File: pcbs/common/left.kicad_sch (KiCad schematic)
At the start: 88 parts

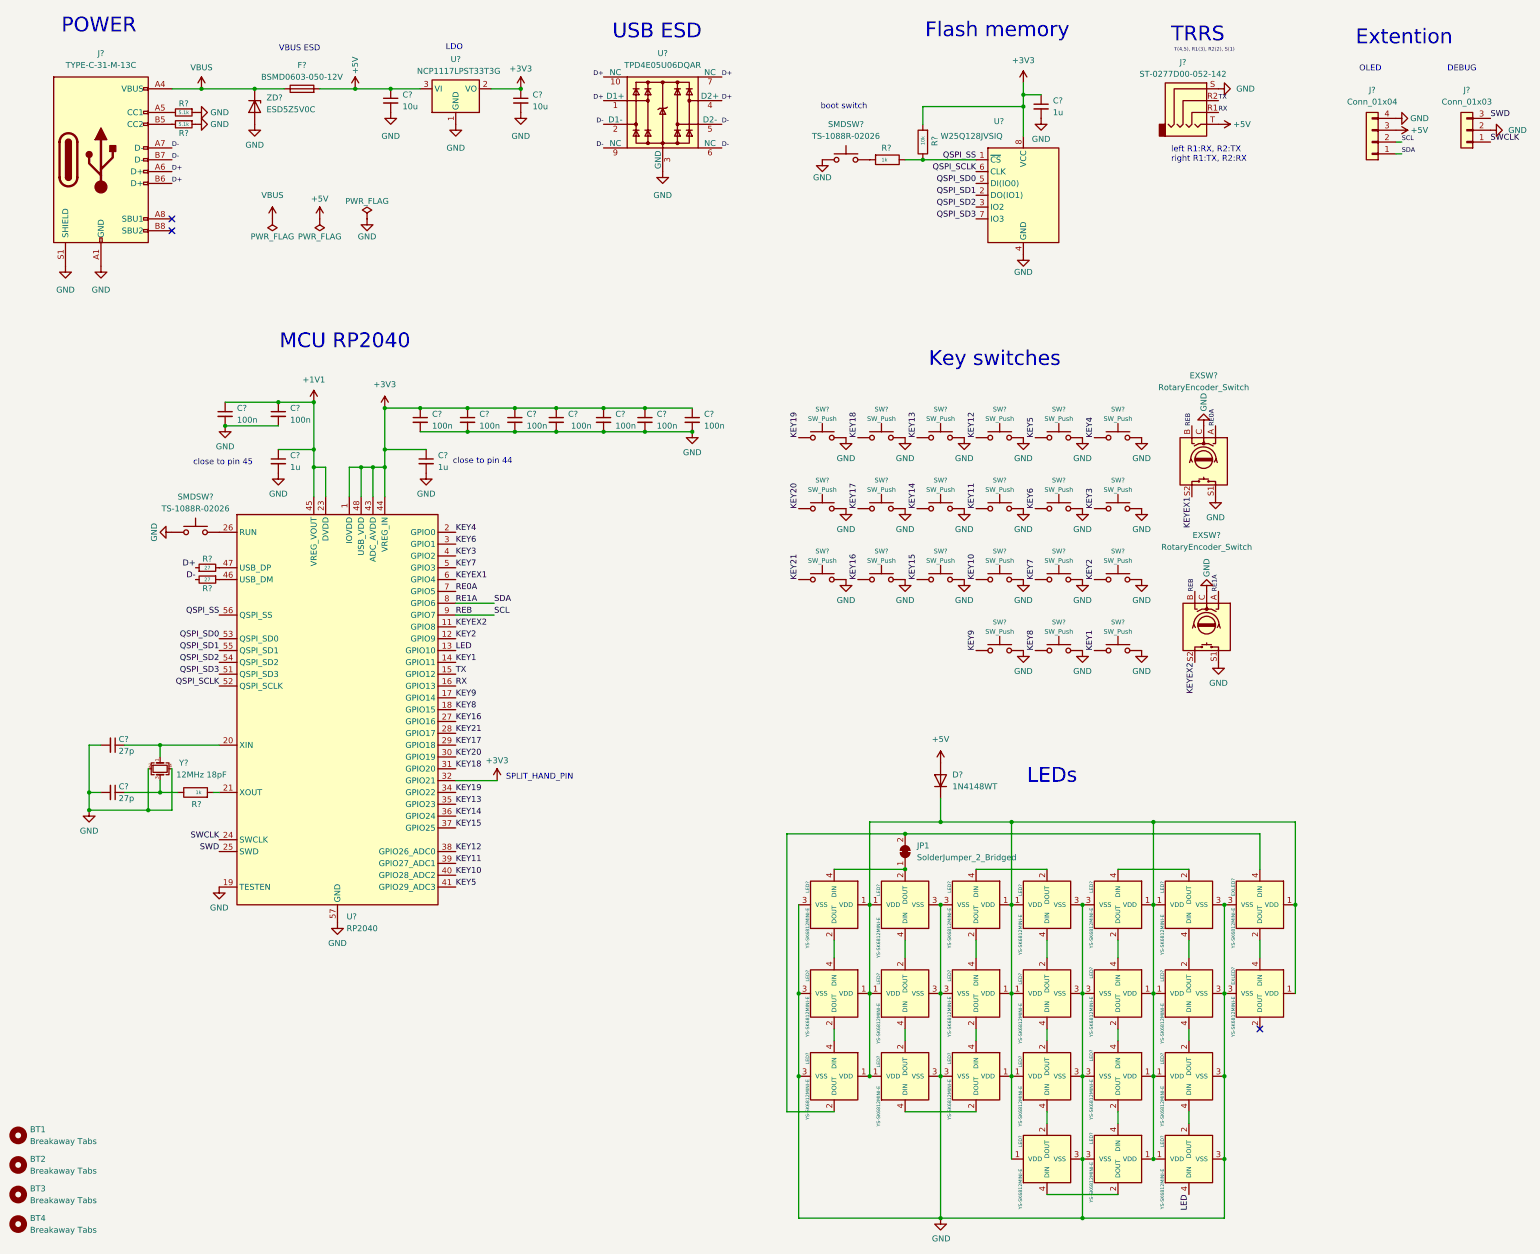
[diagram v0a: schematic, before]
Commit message: Updated pcb for corne-chocolate to use PJ-606-6A audio jack
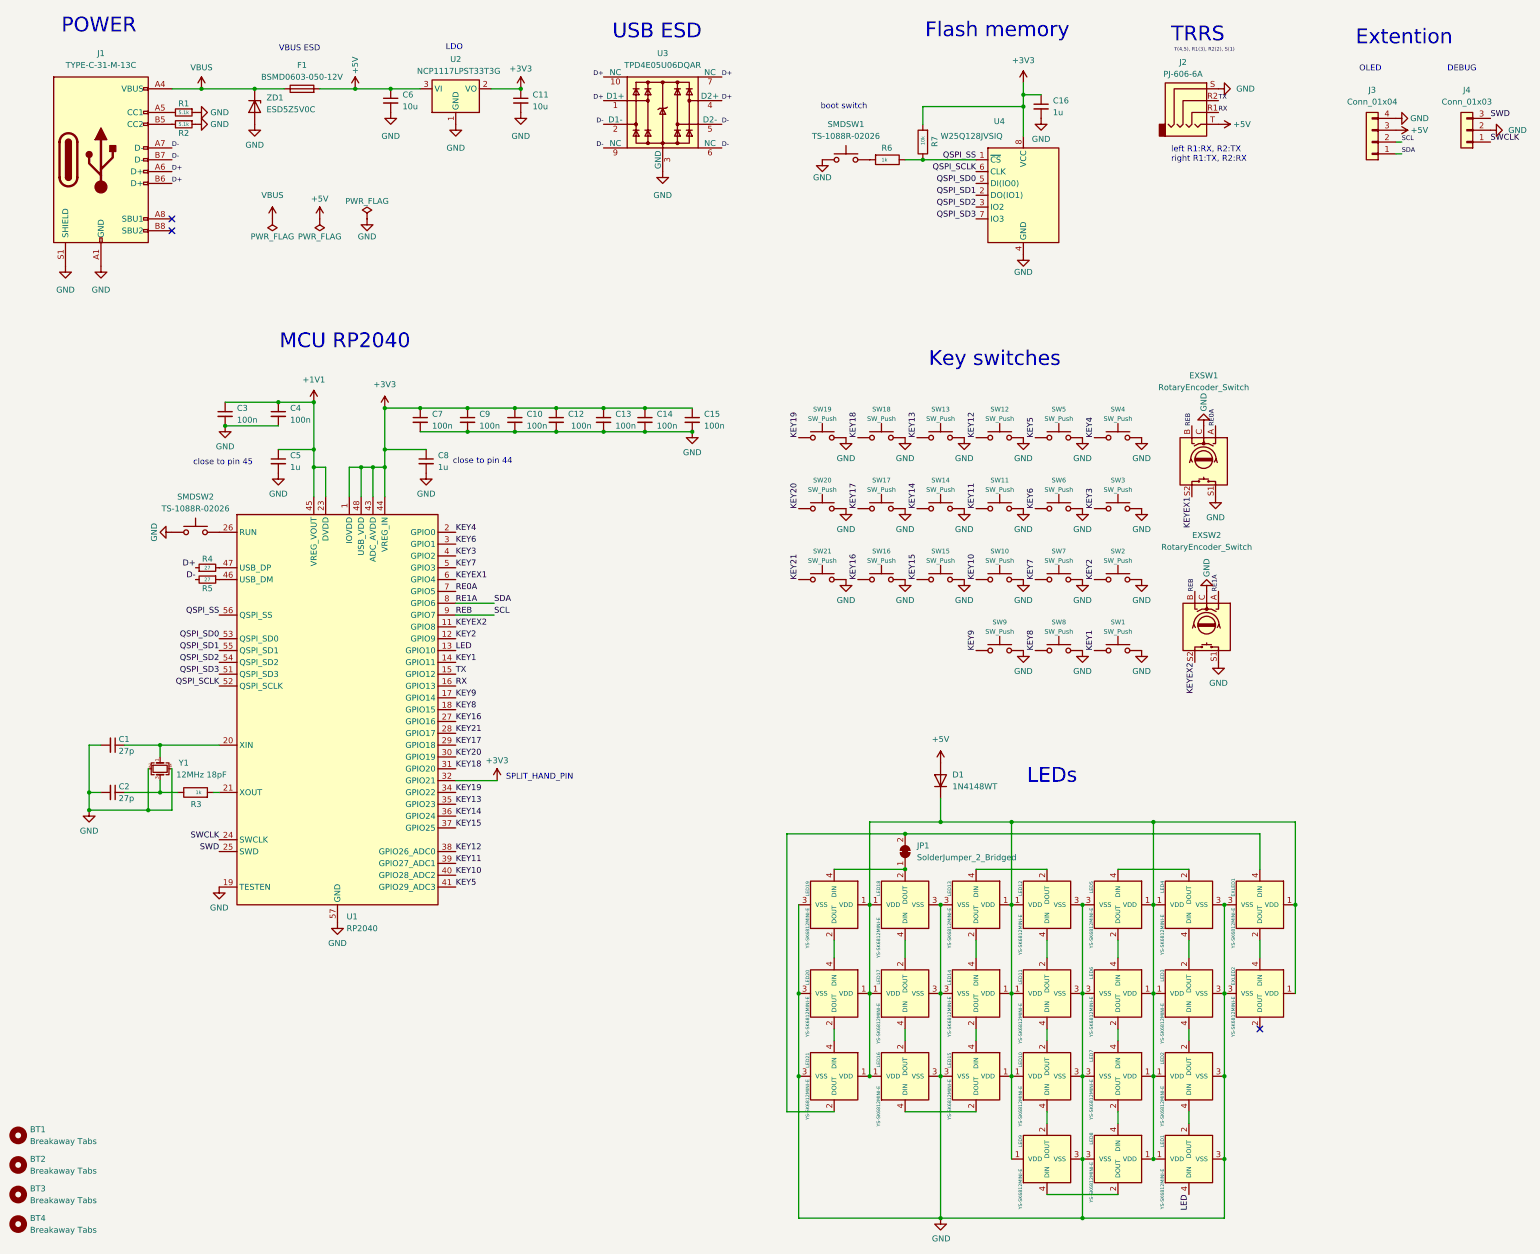
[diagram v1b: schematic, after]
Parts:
- EXLED1, EXLED2: renamed from EXLED?; JLCPCB Part # (none) -> C5149201
- EXSW1, EXSW2: renamed from EXSW?; footprint kbd_local:keyswitch_cherrymx_hotswap_1u_rotary_encoder_ec12 -> kbd_local:keyswitch_choc12_hotswap_1u_rotary_encoder_ec12; JLCPCB Part # (none) -> C5333465
- J2: renamed from J?; value ST-0277D00-052-142 -> PJ-606-6A; footprint kbd_local:ST-0277D00-052-142 -> kbd_local:PJ-606-6A; JLCPCB Part # C2837093 -> C145806
- LED1, LED10, LED11, LED12, LED13, LED14, LED15, LED16, LED17, LED18, LED19, LED2, LED20, LED21, LED3, LED4, LED5, LED6, LED7, LED8, LED9: renamed from LED?; JLCPCB Part # (none) -> C5149201
- SW1: renamed from SW?; footprint kbd:keyswitch_cherrymx_hotswap_1.5u -> kbd_local:keyswitch_choc12_hotswap_1.5u; JLCPCB Part # (none) -> C5333465
- SW10, SW11, SW12, SW13, SW14, SW15, SW16, SW17, SW18, SW19, SW2, SW20, SW21, SW3, SW4, SW5, SW6, SW7, SW8, SW9: renamed from SW?; footprint kbd:keyswitch_cherrymx_hotswap_1u -> kbd_local:keyswitch_choc12_hotswap_1u; JLCPCB Part # (none) -> C5333465
- gave numbers to parts that had none: 36
